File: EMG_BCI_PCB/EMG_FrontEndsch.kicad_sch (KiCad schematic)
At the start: 22 parts, among them U1 INA350, U2 ADA4807-4ARUZ

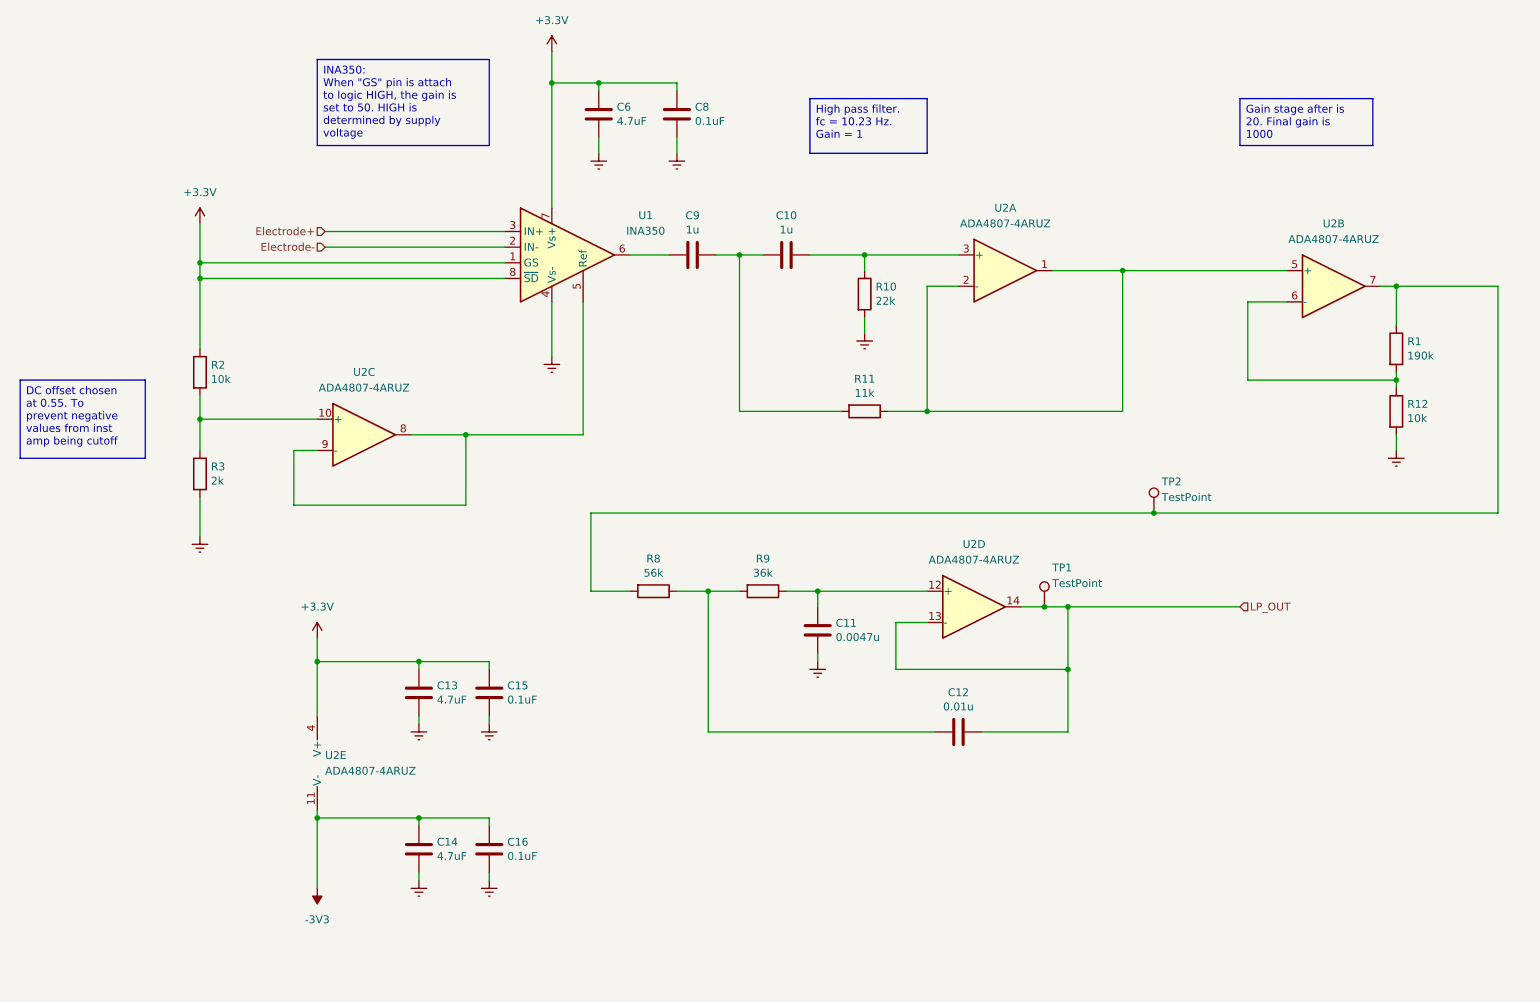
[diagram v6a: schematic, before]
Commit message: Initial placement and routing
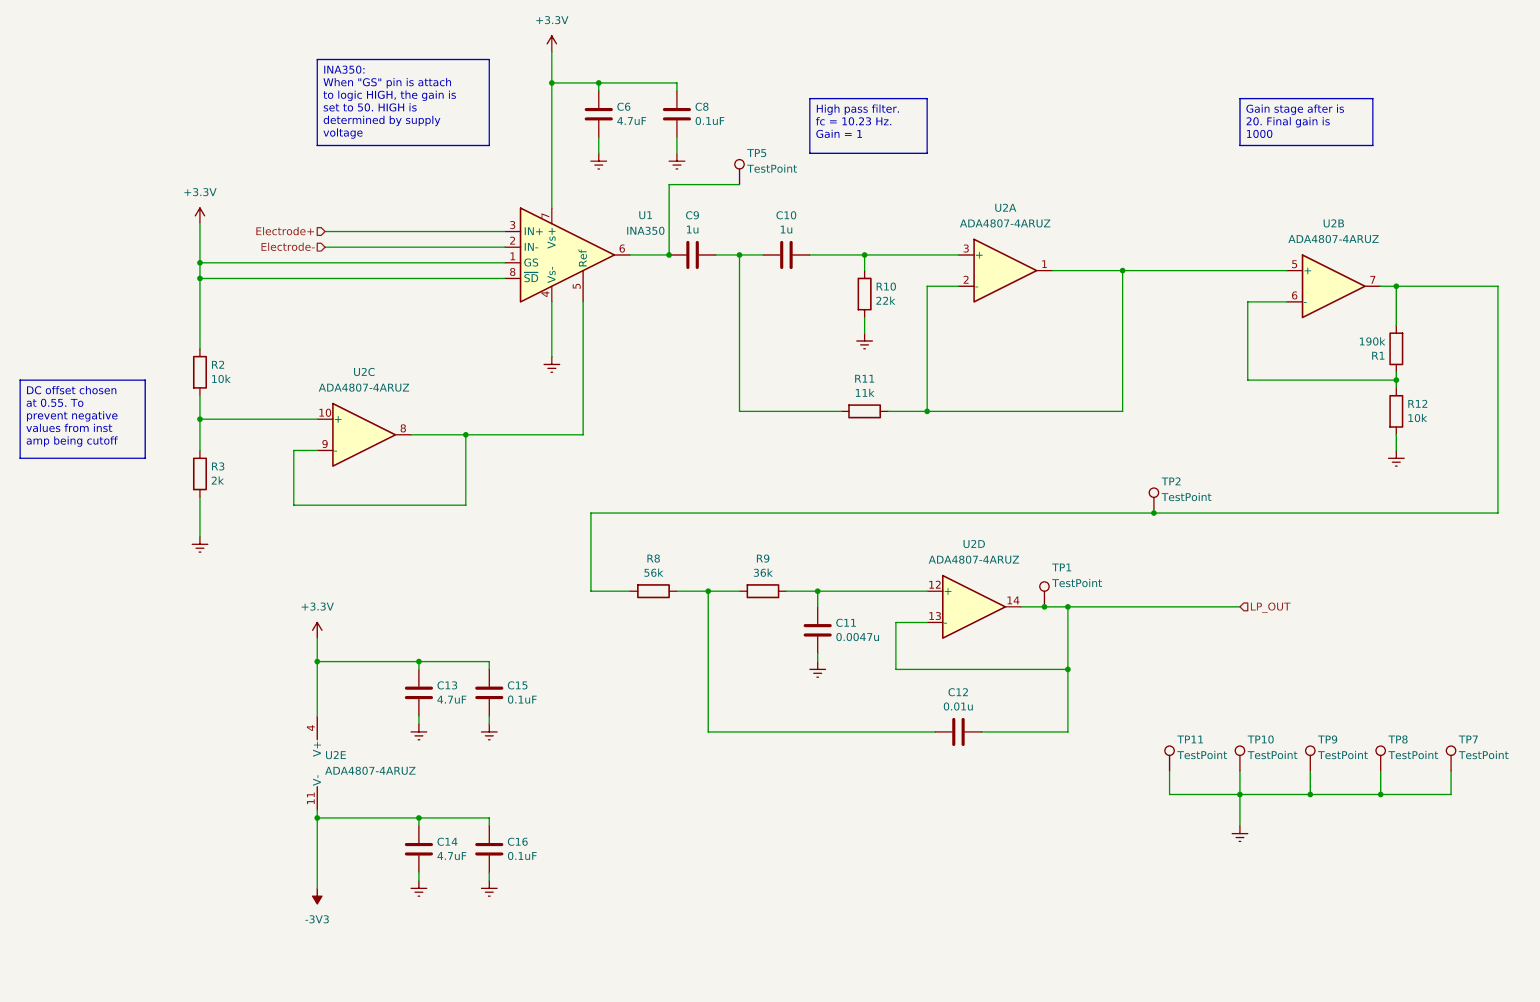
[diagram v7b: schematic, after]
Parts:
- added TP10, TP11, TP5, TP7, TP8, TP9: TestPoint, Connector_PinHeader_2.54mm:PinHeader_1x01_P2.54mm_Vertical, symbol Connector:TestPoint
- C10, C11, C12, C13, C14, C15, C16, C6, C8, C9: footprint Capacitor_SMD:C_0201_0603Metric_Pad0.64x0.40mm_HandSolder -> Capacitor_SMD:C_0603_1608Metric_Pad1.08x0.95mm_HandSolder
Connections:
- net Earth: now also TP10.1, TP11.1, TP7.1, TP8.1, TP9.1
- net at C9.2, U1.6: now also TP5.1
- net at R12.1, U2.6 (-): now also R1.1; no longer R1.2
- net at R8.2, TP2.1, U2.7: now also R1.2; no longer R1.1
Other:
- moved on the sheet: R1

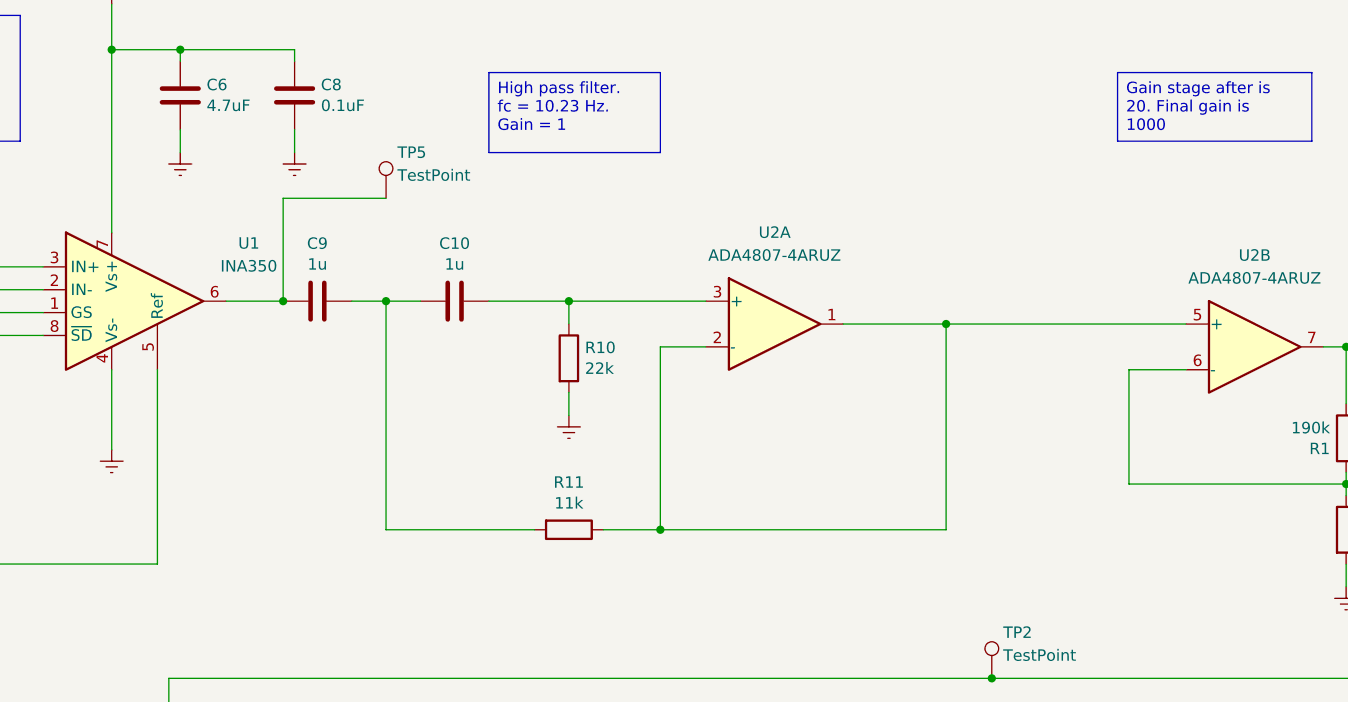
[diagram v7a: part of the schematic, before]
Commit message: Ordering the components
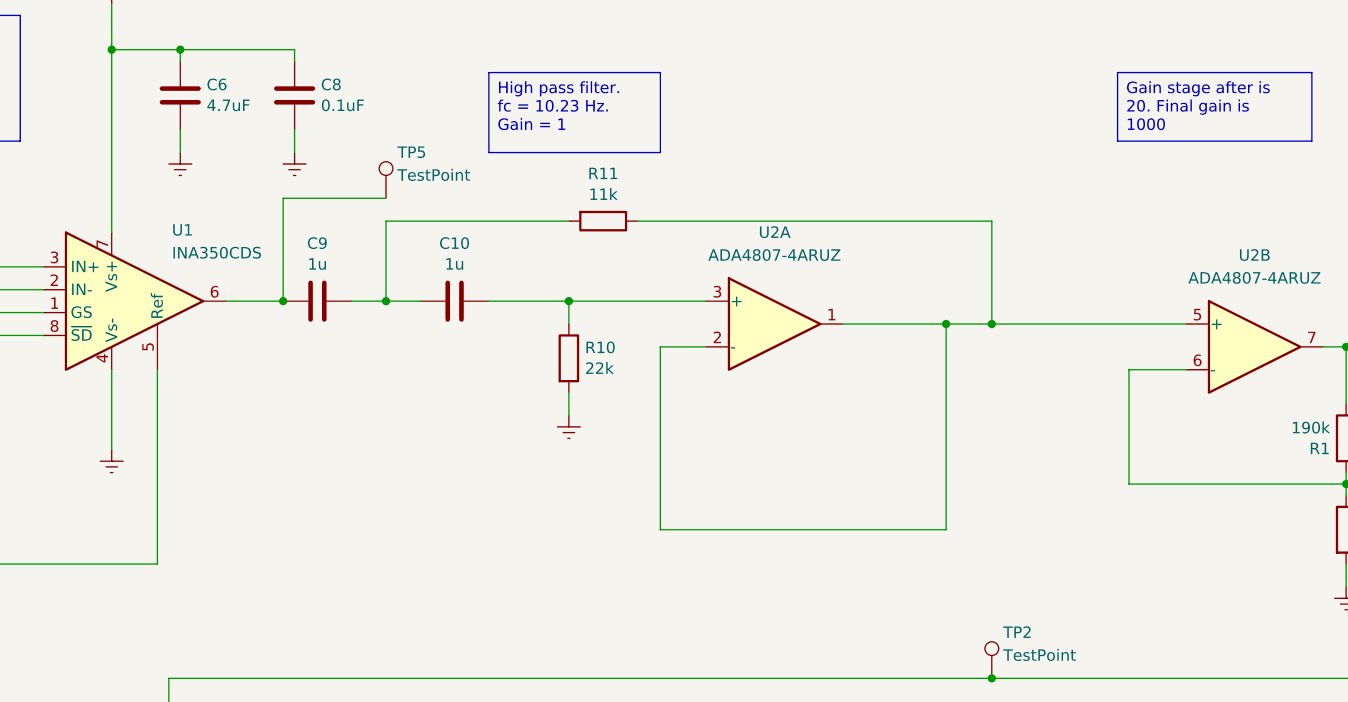
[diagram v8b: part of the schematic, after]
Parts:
- U1: value INA350 -> INA350CDS
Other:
- moved on the sheet: R11
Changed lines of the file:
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@@
+	)
+	(junction
+		(at 215.9 57.15)
+		(diameter 0)
+		(color 0 0 0 0)
 	)
 	(junction
@@
 	)
 	(junction
-		(at 179.07 80.01)
-		(diameter 0)
-		(color 0 0 0 0)
-	)
-	(junction
 		(at 252.73 142.24)
 		(diameter 0)
@@
 	(wire
 		(pts
-			(xy 172.72 80.01) (xy 179.07 80.01)
+			(xy 176.53 45.72) (xy 215.9 45.72)
 		)
 		(stroke
@@
 	(wire
 		(pts
+			(xy 215.9 57.15) (xy 237.49 57.15)
+		)
+		(stroke
+			(width 0)
+			(type default)
+		)
+	)
+	(wire
+		(pts
 			(xy 107.95 146.05) (xy 96.52 146.05)
 		)
@@
 	(wire
 		(pts
-			(xy 165.1 80.01) (xy 148.59 80.01)
+			(xy 168.91 45.72) (xy 148.59 45.72)
 		)
 		(stroke
@@
 	(wire
 		(pts
-			(xy 148.59 54.61) (xy 148.59 80.01)
+			(xy 148.59 45.72) (xy 148.59 54.61)
 		)
 		(stroke
@@
 	(wire
 		(pts
+			(xy 215.9 45.72) (xy 215.9 57.15)
+		)
+		(stroke
+			(width 0)
+			(type default)
+		)
+	)
+	(wire
+		(pts
 			(xy 264.16 138.43) (xy 264.16 142.24)
 		)
@@
 	(wire
 		(pts
-			(xy 210.82 57.15) (xy 237.49 57.15)
+			(xy 210.82 57.15) (xy 215.9 57.15)
 		)
 		(stroke
@@
 	(wire
 		(pts
+			(xy 95.25 83.82) (xy 104.14 83.82)
+		)
+		(stroke
+			(width 0)
+			(type default)
+		)
+	)
+	(wire
+		(pts
+			(xy 168.91 54.61) (xy 168.91 57.15)
+		)
+		(stroke
+			(width 0)
+			(type default)
+		)
+	)
+	(wire
+		(pts
+			(xy 252.73 138.43) (xy 252.73 142.24)
+		)
+		(stroke
+			(width 0)
+			(type default)
+		)
+	)
+	(wire
+		(pts
+			(xy 252.73 142.24) (xy 241.3 142.24)
+		)
+		(stroke
+			(width 0)
+			(type default)
+		)
+	)
+	(wire
+		(pts
+			(xy 173.99 114.3) (xy 179.07 114.3)
+		)
+		(stroke
+			(width 0)
+			(type default)
+		)
+	)
+	(wire
+		(pts
+			(xy 125.73 38.1) (xy 125.73 35.56)
+		)
+		(stroke
+			(width 0)
+			(type default)
+		)
+	)
+	(wire
+		(pts
+			(xy 210.82 57.15) (xy 210.82 80.01)
+		)
+		(stroke
+			(width 0)
+			(type default)
+		)
+	)
+	(wire
+		(pts
+			(xy 201.93 132.08) (xy 187.96 132.08)
+		)
+		(stroke
+			(width 0)
+			(type default)
+		)
+	)
+	(wire
+		(pts
+			(xy 118.11 26.67) (xy 118.11 46.99)
+		)
+		(stroke
+			(width 0)
+			(type default)
+		)
+	)
+	(wire
+		(pts
 			(xy 179.07 59.69) (xy 179.07 80.01)
-		)
-		(stroke
-			(width 0)
-			(type default)
-		)
-	)
-	(wire
-		(pts
-			(xy 95.25 83.82) (xy 104.14 83.82)
-		)
-		(stroke
-			(width 0)
-			(type default)
-		)
-	)
-	(wire
-		(pts
-			(xy 168.91 54.61) (xy 168.91 57.15)
-		)
-		(stroke
-			(width 0)
-			(type default)
-		)
-	)
-	(wire
-		(pts
-			(xy 252.73 138.43) (xy 252.73 142.24)
-		)
-		(stroke
-			(width 0)
-			(type default)
-		)
-	)
-	(wire
-		(pts
-			(xy 252.73 142.24) (xy 241.3 142.24)
-		)
-		(stroke
-			(width 0)
-			(type default)
-		)
-	)
-	(wire
-		(pts
-			(xy 173.99 114.3) (xy 179.07 114.3)
-		)
-		(stroke
-			(width 0)
-			(type default)
-		)
-	)
-	(wire
-		(pts
-			(xy 125.73 38.1) (xy 125.73 35.56)
-		)
-		(stroke
-			(width 0)
-			(type default)
-		)
-	)
-	(wire
-		(pts
-			(xy 210.82 57.15) (xy 210.82 80.01)
-		)
-		(stroke
-			(width 0)
-			(type default)
-		)
-	)
-	(wire
-		(pts
-			(xy 201.93 132.08) (xy 187.96 132.08)
-		)
-		(stroke
-			(width 0)
-			(type default)
-		)
-	)
-	(wire
-		(pts
-			(xy 118.11 26.67) (xy 118.11 46.99)
 		)
 		(stroke
@@
 	(symbol
 		(lib_id "Device:R")
-		(at 168.91 80.01 270)
+		(at 172.72 45.72 270)
 		(unit 1)
 		(exclude_from_sim no)
@@
 		(dnp no)
 		(property "Reference" "R11"
-			(at 168.91 74.7522 90)
+			(at 172.72 40.4622 90)
 			(effects
 				(font
@@
 		)
 		(property "Value" "11k"
-			(at 168.91 77.0636 90)
+			(at 172.72 42.7736 90)
 			(effects
 				(font
@@
 		)
 		(property "Footprint" "Resistor_SMD:R_0603_1608Metric_Pad0.98x0.95mm_HandSolder"
-			(at 168.91 78.232 90)
+			(at 172.72 43.942 90)
 			(effects
 				(font
@@
 		)
 		(property "Datasheet" "~"
-			(at 168.91 80.01 0)
+			(at 172.72 45.72 0)
 			(effects
 				(font
@@
 		)
 		(property "Description" ""
-			(at 168.91 80.01 0)
+			(at 172.72 45.72 0)
 			(effects
 				(font
@@
 		(on_board yes)
 		(dnp no)
-		(fields_autoplaced yes)
 		(property "Reference" "U1"
-			(at 133.35 48.1898 0)
-			(effects
-				(font
-					(size 1.27 1.27)
-				)
-			)
-		)
-		(property "Value" "INA350"
-			(at 133.35 50.7298 0)
-			(effects
-				(font
+			(at 125.984 46.736 0)
+			(effects
+				(font
+					(size 1.27 1.27)
+				)
+			)
+		)
+		(property "Value" "INA350CDS"
+			(at 129.794 49.276 0)
+			(effects
+				(font
